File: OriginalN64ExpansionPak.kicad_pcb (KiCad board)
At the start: 2 copper layers, 41.9 x 21 mm, 14 parts, among them U1 MSM5718B70-60GS-K, U2 Expansion Pak Edge Connector

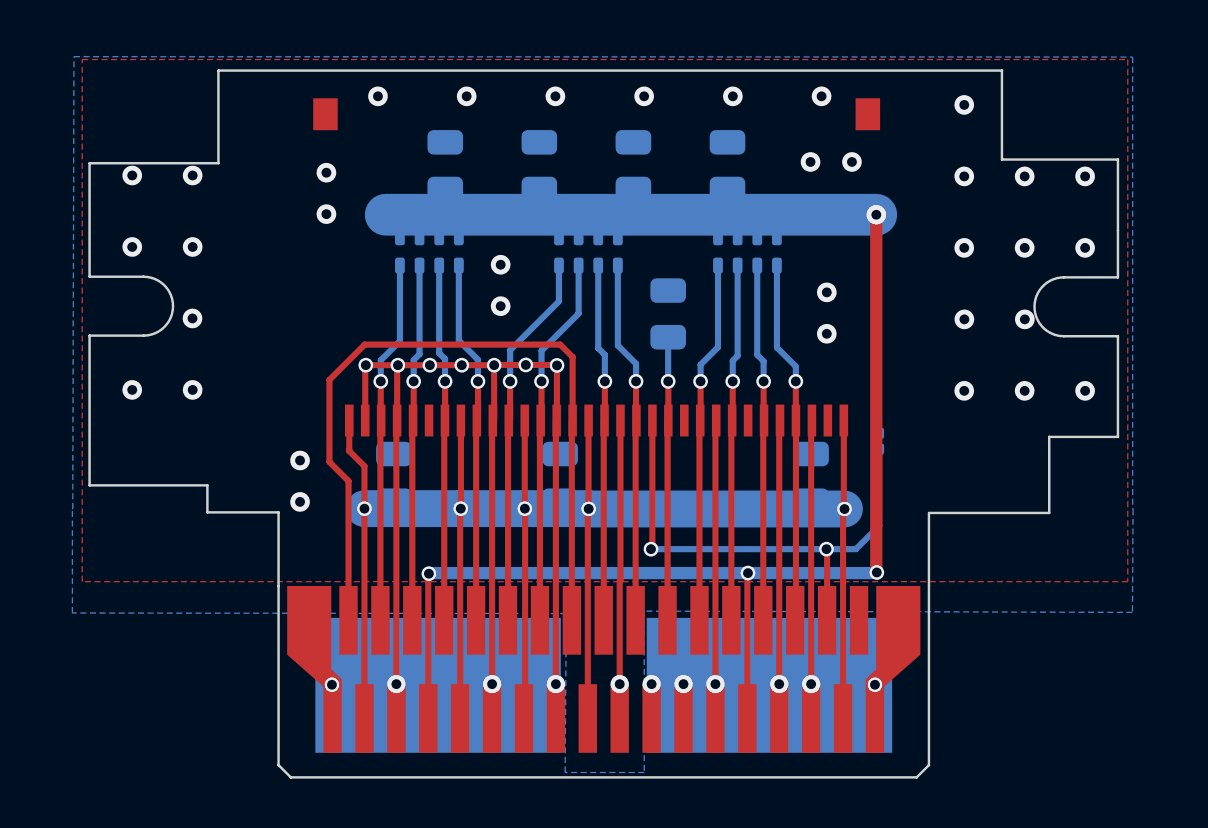
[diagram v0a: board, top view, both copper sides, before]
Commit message: Updating R13 to have a larger package size so it's easier to solder by hand
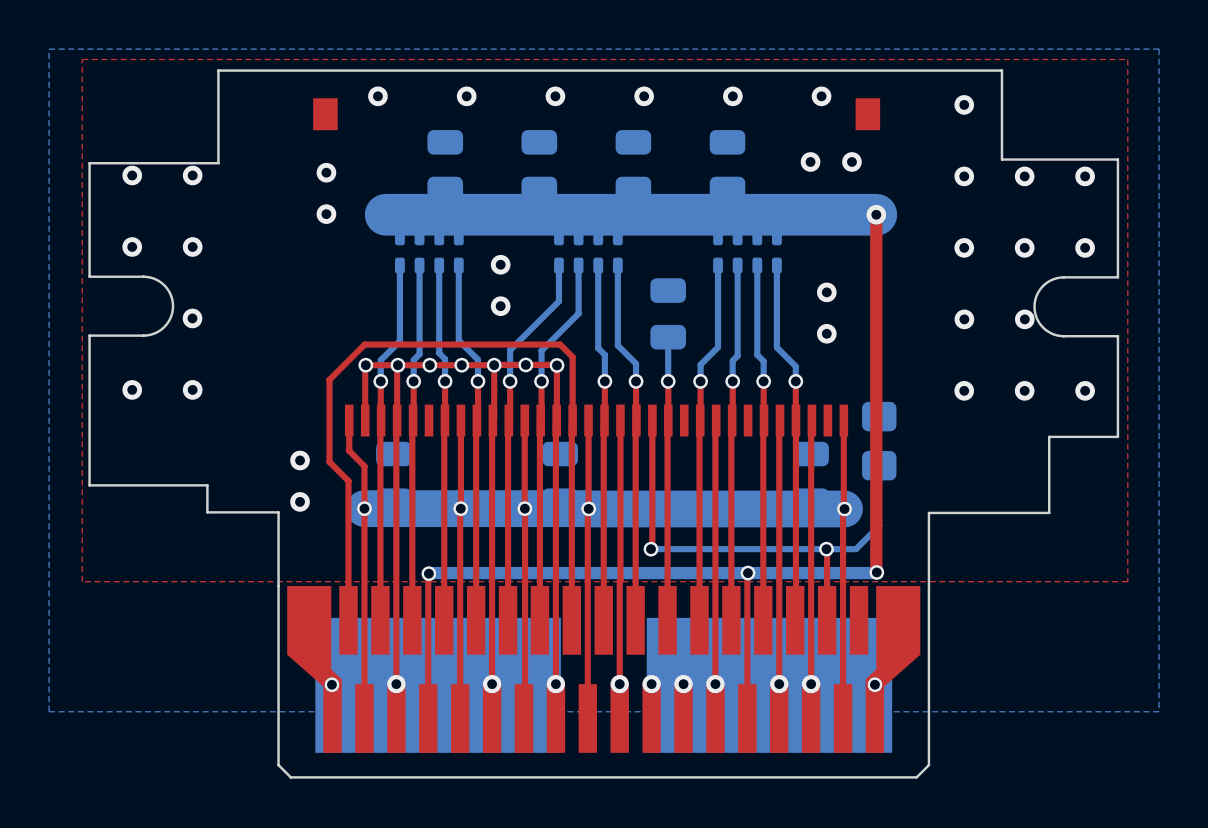
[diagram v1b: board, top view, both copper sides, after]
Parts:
- R13: value Yageo RC0603FR-07510RL -> Yageo RC0805FR-07510RL; footprint Resistor_SMD:R_0201_0603Metric -> Resistor_SMD:R_0805_2012Metric_Pad1.20x1.40mm_HandSolder
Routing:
- net Net-(R13-Pad2): track 21.0 -> 20.3 mm
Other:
- outline, holes or cut-outs redrawn
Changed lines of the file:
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@@
     )
   )
-  (footprint "Resistor_SMD:R_0201_0603Metric" (layer "B.Cu")
+  (footprint "Resistor_SMD:R_0805_2012Metric_Pad1.20x1.40mm_HandSolder" (layer "B.Cu")
     (at 147.85 95.225 -90)
-    (descr "Resistor SMD 0201 (0603 Metric), square (rectangular) end terminal, IPC_7351 nominal, (Body size source: https://www.vishay.com/docs/20052/crcw0201e3.pdf), generated with kicad-footprint-generator")
-    (tags "resistor")
+    (descr "Resistor SMD 0805 (2012 Metric), square (rectangular) end terminal, IPC_7351 nominal with elongated pad for handsoldering. (Body size source: IPC-SM-782 page 72, https://www.pcb-3d.com/wordpress/wp-content/uploads/ipc-sm-782a_amendment_1_and_2.pdf), generated with kicad-footprint-generator")
+    (tags "resistor handsolder")
     (property "CASE/PACKAGE" "0603")
     (property "LEAD-FREE STATUS" "Lead Free")
@@
     (property "MOUNTING STYLE" "Surface Mount")
     (property "NUMBER OF PINS" "2")
-    (property "OCTOPART URL" "http://octopart.com/rc0603fr-07510rl-yageo-1403392")
+    (property "OCTOPART URL" "https://octopart.com/rc0805fr-07510rl-yageo-1169945?r=sp")
     (property "OCTOPARTID" "c4ff0de08b991b38")
     (property "PACKAGING" "Tape & Reel (TR), Cut Tape (CT)")
@@
     (property "VOLTAGE RATING (DC)" "50.0 V")
     (attr smd)
-    (fp_text reference "R13" (at -0.025 -1.375 90) (layer "B.SilkS")
+    (fp_text reference "R13" (at -3.65 0 90) (layer "B.SilkS")
       (effects (font (size 1 1) (thickness 0.15)) (justify mirror))
     )
-    (fp_text value "Yageo RC0603FR-07510RL" (at 0 -1.05 90) (layer "B.Fab") hide
+    (fp_text value "Yageo RC0805FR-07510RL" (at 0 -1.65 90) (layer "B.Fab") hide
       (effects (font (size 1 1) (thickness 0.15)) (justify mirror))
     )
-    (fp_text user "${REFERENCE}" (at 0 0.68 90) (layer "B.Fab")
-      (effects (font (size 0.25 0.25) (thickness 0.04)) (justify mirror))
+    (fp_text user "${REFERENCE}" (at 0 0 90) (layer "B.Fab") hide
+      (effects (font (size 0.5 0.5) (thickness 0.08)) (justify mirror))
     )
-    (fp_line (start -0.7 -0.35) (end -0.7 0.35) (layer "B.CrtYd") (width 0.05))
-    (fp_line (start 0.7 0.35) (end 0.7 -0.35) (layer "B.CrtYd") (width 0.05))
-    (fp_line (start 0.7 -0.35) (end -0.7 -0.35) (layer "B.CrtYd") (width 0.05))
-    (fp_line (start -0.7 0.35) (end 0.7 0.35) (layer "B.CrtYd") (width 0.05))
-    (fp_line (start -0.3 0.15) (end 0.3 0.15) (layer "B.Fab") (width 0.1))
-    (fp_line (start 0.3 0.15) (end 0.3 -0.15) (layer "B.Fab") (width 0.1))
-    (fp_line (start 0.3 -0.15) (end -0.3 -0.15) (layer "B.Fab") (width 0.1))
-    (fp_line (start -0.3 -0.15) (end -0.3 0.15) (layer "B.Fab") (width 0.1))
-    (pad "" smd roundrect (at -0.345 0 270) (size 0.318 0.36) (layers "B.Paste") (roundrect_rratio 0.25))
-    (pad "" smd roundrect (at 0.345 0 270) (size 0.318 0.36) (layers "B.Paste") (roundrect_rratio 0.25))
-    (pad "1" smd roundrect (at -0.32 0 270) (size 0.46 0.4) (layers "B.Cu" "B.Mask") (roundrect_rratio 0.25)
+    (fp_line (start -0.227064 0.735) (end 0.227064 0.735) (layer "B.SilkS") (width 0.12))
+    (fp_line (start -0.227064 -0.735) (end 0.227064 -0.735) (layer "B.SilkS") (width 0.12))
+    (fp_line (start 1.85 -0.95) (end -1.85 -0.95) (layer "B.CrtYd") (width 0.05))
+    (fp_line (start -1.85 0.95) (end 1.85 0.95) (layer "B.CrtYd") (width 0.05))
+    (fp_line (start 1.85 0.95) (end 1.85 -0.95) (layer "B.CrtYd") (width 0.05))
+    (fp_line (start -1.85 -0.95) (end -1.85 0.95) (layer "B.CrtYd") (width 0.05))
+    (fp_line (start 1 0.625) (end 1 -0.625) (layer "B.Fab") (width 0.1))
+    (fp_line (start 1 -0.625) (end -1 -0.625) (layer "B.Fab") (width 0.1))
+    (fp_line (start -1 0.625) (end 1 0.625) (layer "B.Fab") (width 0.1))
+    (fp_line (start -1 -0.625) (end -1 0.625) (layer "B.Fab") (width 0.1))
+    (pad "1" smd roundrect (at -1 0 270) (size 1.2 1.4) (layers "B.Cu" "B.Paste" "B.Mask") (roundrect_rratio 0.208333)
       (net 1 "GND") (pinfunction "1") (pintype "passive"))
-    (pad "2" smd roundrect (at 0.32 0 270) (size 0.46 0.4) (layers "B.Cu" "B.Mask") (roundrect_rratio 0.25)
+    (pad "2" smd roundrect (at 1 0 270) (size 1.2 1.4) (layers "B.Cu" "B.Paste" "B.Mask") (roundrect_rratio 0.208333)
       (net 17 "Net-(R13-Pad2)") (pinfunction "2") (pintype "passive"))
-    (model "${KICAD6_3DMODEL_DIR}/Resistor_SMD.3dshapes/R_0201_0603Metric.wrl"
+    (model "${KICAD6_3DMODEL_DIR}/Resistor_SMD.3dshapes/R_0805_2012Metric.wrl"
       (offset (xyz 0 0 0))
       (scale (xyz 1 1 1))
@@
     ) (layer "B.SilkS") (width 0) (fill solid))
   (gr_line (start 123.375 101.125) (end 123.375 98.125) (layer "Edge.Cuts") (width 0.1))
-  (gr_line (start 157.575 86.65) (end 157.575 88.55) (layer "Edge.Cuts") (width 0.1))
   (gr_line (start 157.575 95.05) (end 157.575 90.95) (layer "Edge.Cuts") (width 0.1))
   (gr_line (start 157.575 88.55) (end 155.375 88.55) (layer "Edge.Cuts") (width 0.1))
@@
   (gr_line (start 154.775 95.05) (end 157.575 95.05) (layer "Edge.Cuts") (width 0.1))
   (gr_arc (start 117.875 88.525) (mid 119.075 89.725) (end 117.875 90.925) (layer "Edge.Cuts") (width 0.1))
+  (gr_line (start 157.575 83.75) (end 157.575 88.55) (layer "Edge.Cuts") (width 0.1))
   (gr_line (start 123.375 98.125) (end 120.475 98.125) (layer "Edge.Cuts") (width 0.1))
   (gr_line (start 115.675 97.025) (end 115.675 90.925) (layer "Edge.Cuts") (width 0.1))
@@
   (gr_arc (start 155.375 90.95) (mid 154.175 89.75) (end 155.375 88.55) (layer "Edge.Cuts") (width 0.1))
   (gr_line (start 120.925 83.9) (end 120.925 80.125) (layer "Edge.Cuts") (width 0.1))
-  (gr_line (start 157.575 83.75) (end 157.575 86.65) (layer "Edge.Cuts") (width 0.1))
   (gr_line (start 154.775 98.15) (end 154.775 95.05) (layer "Edge.Cuts") (width 0.1))
   (gr_text "LambBrainz.com" (at 139.7101 98.938578) (layer "B.SilkS")
@@
   )
   (segment (start 134.7 92.12) (end 134.72 92.14) (width 0.25) (layer "F.Cu") (net 1))
+  (segment (start 145.075 106.525) (end 145.075 94.416) (width 0.25) (layer "F.Cu") (net 1))
   (segment (start 134.675 94.416) (end 134.706 94.385) (width 0.25) (layer "F.Cu") (net 1))
   (segment (start 132.106 94.385) (end 132.16 94.331) (width 0.25) (layer "F.Cu") (net 1))
@@
   (segment (start 126.915 92.145) (end 126.906 92.154) (width 0.25) (layer "F.Cu") (net 1))
   (segment (start 128.175 106.525) (end 128.175 94.416) (width 0.25) (layer "F.Cu") (net 1))
-  (segment (start 145.075 106.525) (end 145.075 94.416) (width 0.25) (layer "F.Cu") (net 1))
   (segment (start 129.54 92.13) (end 128.238543 92.13) (width 0.25) (layer "F.Cu") (net 1))
   (segment (start 128.206 94.385) (end 128.206 92.162543) (width 0.25) (layer "F.Cu") (net 1))
   (segment (start 132.16 92.13) (end 130.84 92.13) (width 0.25) (layer "F.Cu") (net 1))
   (segment (start 137.306 100.894) (end 137.306 94.385) (width 0.25) (layer "F.Cu") (net 1))
-  (segment (start 145.075 94.416) (end 145.106 94.385) (width 0.25) (layer "F.Cu") (net 1))
   (segment (start 132.075 94.416) (end 132.106 94.385) (width 0.25) (layer "F.Cu") (net 1))
   (segment (start 126.906 92.154) (end 126.906 94.385) (width 0.25) (layer "F.Cu") (net 1))
@@
   (segment (start 137.275 106.525) (end 137.275 100.925) (width 0.25) (layer "F.Cu") (net 1))
   (segment (start 134.715 92.145) (end 134.72 92.14) (width 0.25) (layer "F.Cu") (net 1))
+  (segment (start 145.075 94.416) (end 145.106 94.385) (width 0.25) (layer "F.Cu") (net 1))
   (segment (start 141.175 94.416) (end 141.206 94.385) (width 0.25) (layer "F.Cu") (net 1))
   (via (at 151.3125 81.525) (size 0.8) (drill 0.4) (layers "F.Cu" "B.Cu") (free) (net 1))
@@
   (via (at 145.7 99.625) (size 0.6) (drill 0.4) (layers "F.Cu" "B.Cu") (free) (net 17))
   (via (at 138.5495 99.625) (size 0.6) (drill 0.4) (layers "F.Cu" "B.Cu") (free) (net 17))
+  (segment (start 145.7 99.625) (end 138.5495 99.625) (width 0.25) (layer "B.Cu") (net 17))
   (segment (start 146.9 99.625) (end 147.85 98.675) (width 0.25) (layer "B.Cu") (net 17))
   (segment (start 145.7 99.625) (end 146.9 99.625) (width 0.25) (layer "B.Cu") (net 17))
-  (segment (start 145.7 99.625) (end 138.5495 99.625) (width 0.25) (layer "B.Cu") (net 17))
-  (segment (start 147.85 98.675) (end 147.85 95.545) (width 0.25) (layer "B.Cu") (net 17))
+  (segment (start 147.85 98.675) (end 147.85 96.225) (width 0.25) (layer "B.Cu") (net 17))
   (segment (start 126.225 102.525) (end 126.225 96.85) (width 0.25) (layer "F.Cu") (net 19))
   (segment (start 135.325 94.416) (end 135.356 94.385) (width 0.25) (layer "F.Cu") (net 19))
@@
   (zone (net 1) (net_name "GND") (layer "B.Cu") (hatch edge 0.508)
     (connect_pads (clearance 0.1))
-    (min_thickness 0.1) (filled_areas_thickness no)
+    (min_thickness 0.254) (filled_areas_thickness no)
     (fill yes (thermal_gap 0.508) (thermal_bridge_width 0.508))
     (polygon
       (pts
-        (xy 158.175 97.95)
-        (xy 158.191373 98.000247)
-        (xy 158.166373 102.200247)
-        (xy 138.275 102.15)
-        (xy 138.275 108.725)
-        (xy 135.05 108.725)
-        (xy 135.1 102.25)
-        (xy 114.975 102.225)
-        (xy 114.975 98)
-        (xy 114.989354 97.984327)
-        (xy 115.039545 79.559309)
-        (xy 158.175191 79.574982)
+        (xy 159.25 106.25)
+        (xy 114.025 106.25)
+        (xy 114.025 79.25)
+        (xy 159.25 79.25)
       )
     )
